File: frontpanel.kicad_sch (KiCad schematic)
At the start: 17 parts, among them M2 Pico_Display_Pack, Q6 Si2306BDS, SW1 STOP_SW, SW2 Rotary Enc EC11E, U9 MCP23017_SO

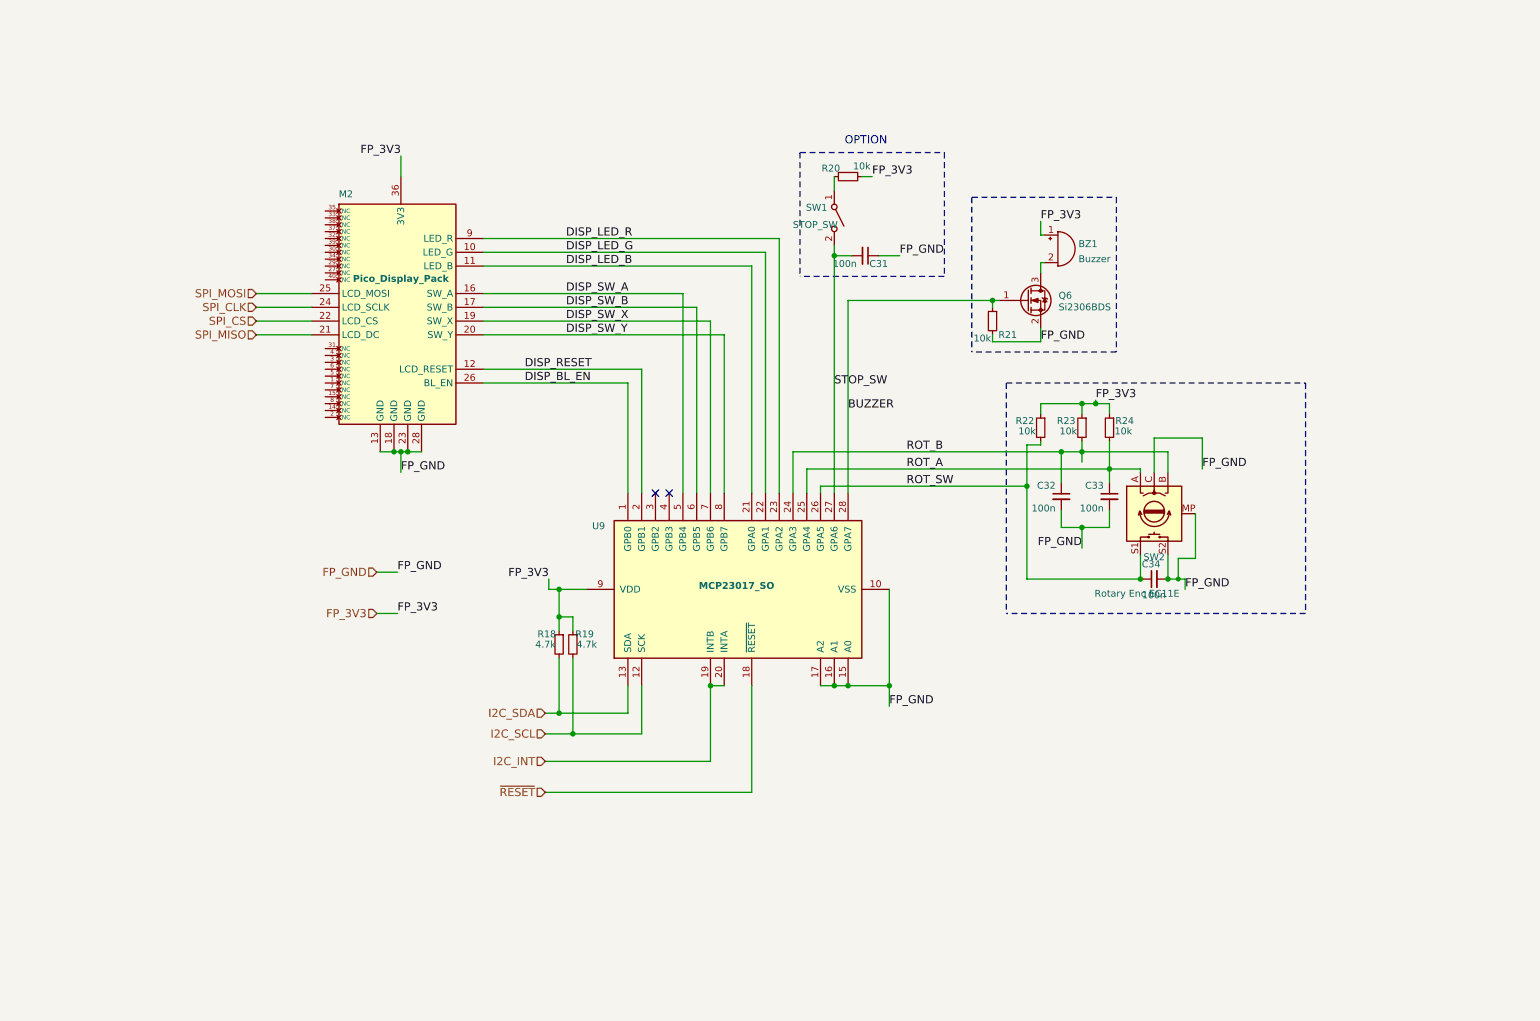
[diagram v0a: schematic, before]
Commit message: Update for Kicad 6-rc; replace 12V reg and cascade; add EEPROM;
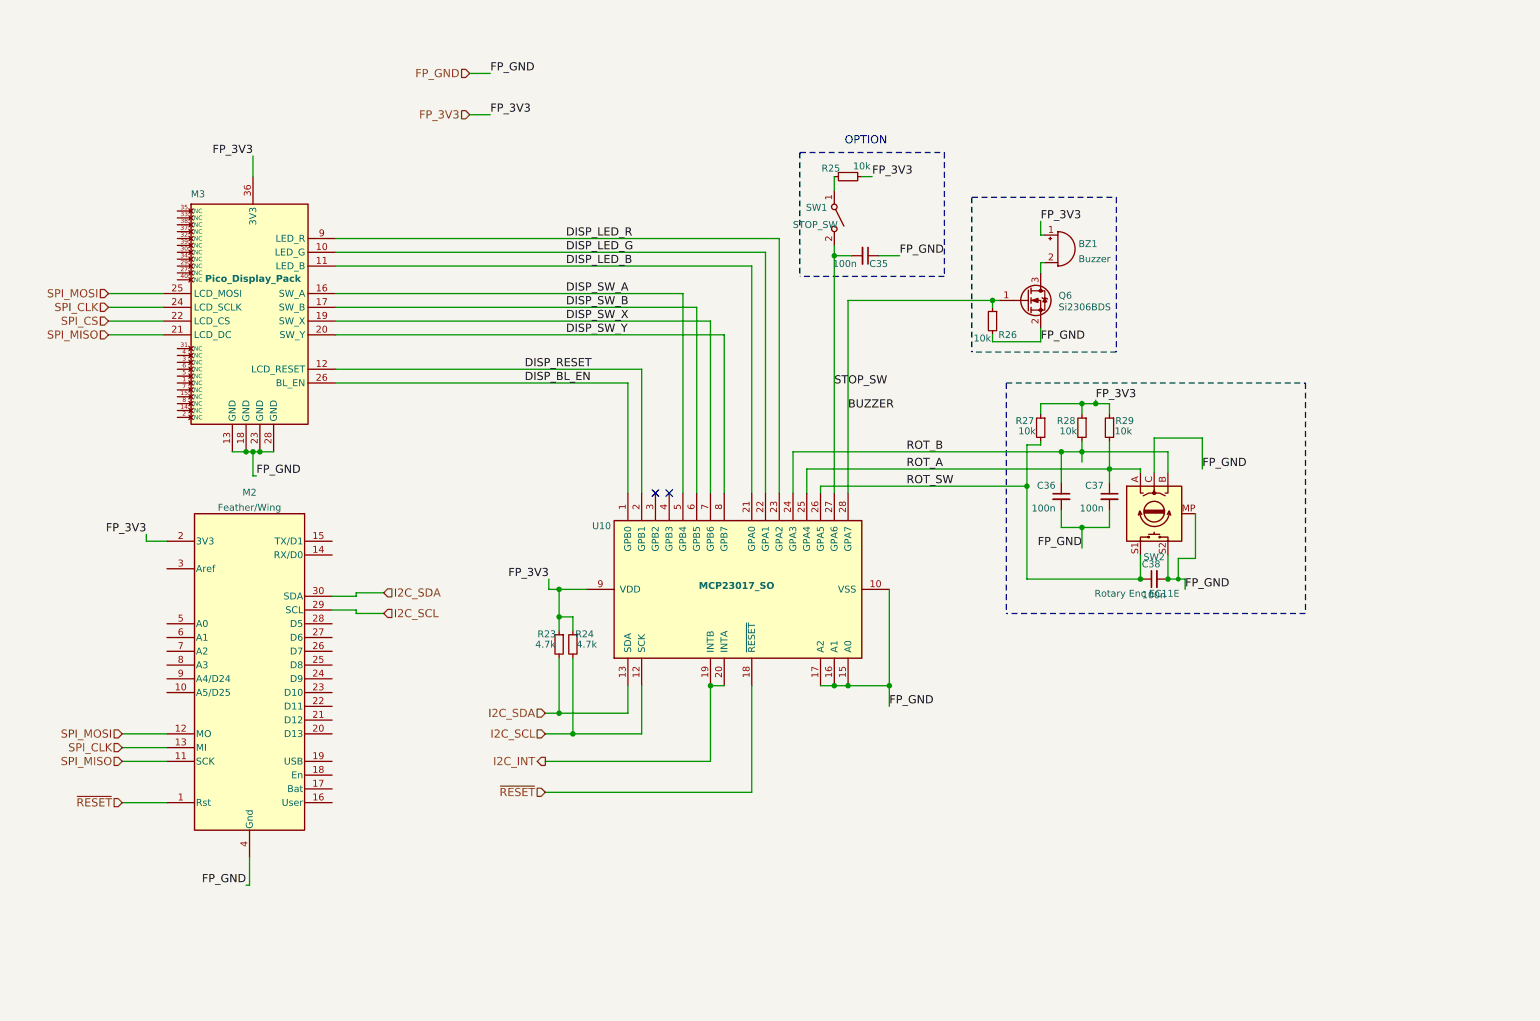
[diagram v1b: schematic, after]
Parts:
- added M2: Feather/Wing, solarpump:FeatherWing_Socket, symbol solarpump:Feather/Wing
- renumbered C31 to C35, C32 to C36, C33 to C37, C34 to C38, M2 to M3, R18 to R23, R19 to R24, R20 to R25, R21 to R26, R22 to R27, R23 to R28, R24 to R29, U9 to U10
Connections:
- net FP_3V3: now also M2.2 (3V3)
- net FP_GND: now also M2.4 (Gnd)
- net I2C_SCL: now also M2.29 (SCL)
- net I2C_SDA: now also M2.30 (SDA)
- net SPI_CLK: now also M2.13 (MI)
- net SPI_MISO: now also M2.11 (SCK)
- net SPI_MOSI: now also M2.12 (MO)
- net ~{RESET}: now also M2.1 (Rst)
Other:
- moved on the sheet: M3

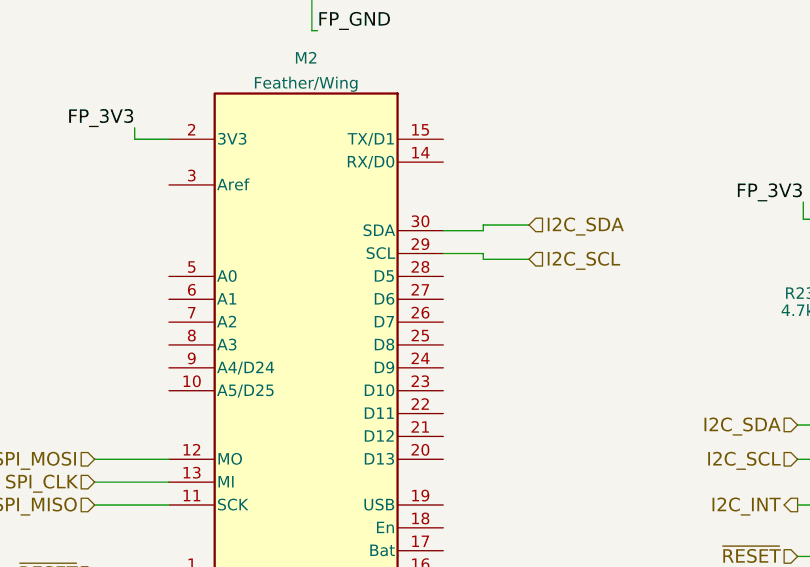
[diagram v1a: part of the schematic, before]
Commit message: Various important tweaks and fixes.
Fix several incorrect capacitor footprints;
Fix slightly incorrect footprint for USB connector;
Add ground vias around MPPT circuit;
Add Zener protection circuit for regulation error input;
Use pin header not socket for Pico Display header;
Fix missing connection to featherwing i2c;
Add in 3d models for USB socket and switch
Update kicad sheet dates;
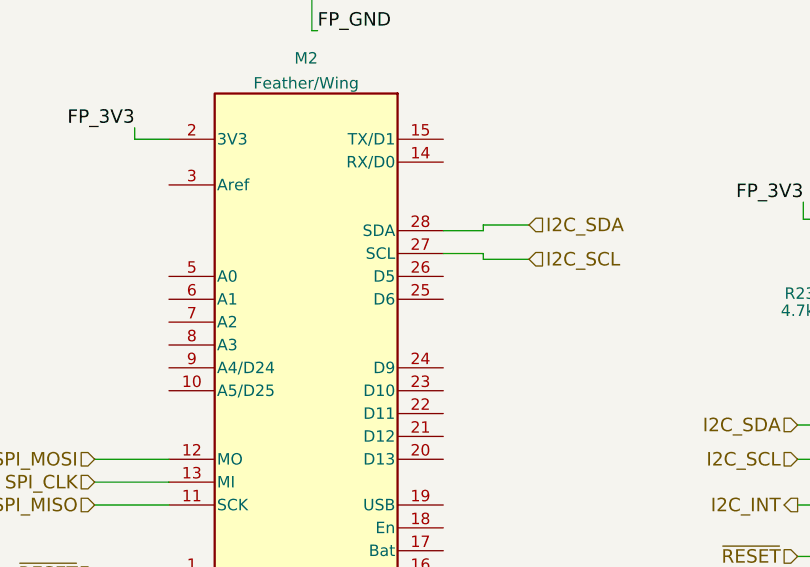
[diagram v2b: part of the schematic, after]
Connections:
- net I2C_SCL: now also M2.27 (SCL); no longer M2.29 (SCL)
- net I2C_SDA: now also M2.28 (SDA); no longer M2.30 (SDA)
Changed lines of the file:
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@@
   (title_block
     (title "SolarPump v3")
-    (date "2021-11-15")
+    (date "2021-12-03")
     (rev "1.0")
     (company "IvimeyCom")
@@
     (pin "27")
     (pin "28")
-    (pin "29")
     (pin "3")
-    (pin "30")
     (pin "4")
     (pin "5")

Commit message: Adjust footprint silkscreen; modify EC11 FP to inset into board, and adjust display board
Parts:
- SW2: footprint Rotary_Encoder:RotaryEncoder_Alps_EC11E-Switch_Vertical_H20mm -> solarpump:RotaryEncoder_Alps_EC11E-Switch_Vertical_H20mm_Inset
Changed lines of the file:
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@@
     (property "Reference" "SW2" (id 0) (at 224.155 113.4068 90))
     (property "Value" "Rotary Enc EC11E" (id 1) (at 220.98 120.1505 90))
-    (property "Footprint" "Rotary_Encoder:RotaryEncoder_Alps_EC11E-Switch_Vertical_H20mm" (id 2) (at 220.345 101.346 0)
+    (property "Footprint" "solarpump:RotaryEncoder_Alps_EC11E-Switch_Vertical_H20mm_Inset" (id 2) (at 220.345 101.346 0)
       (effects (font (size 1.27 1.27)) hide)
     )

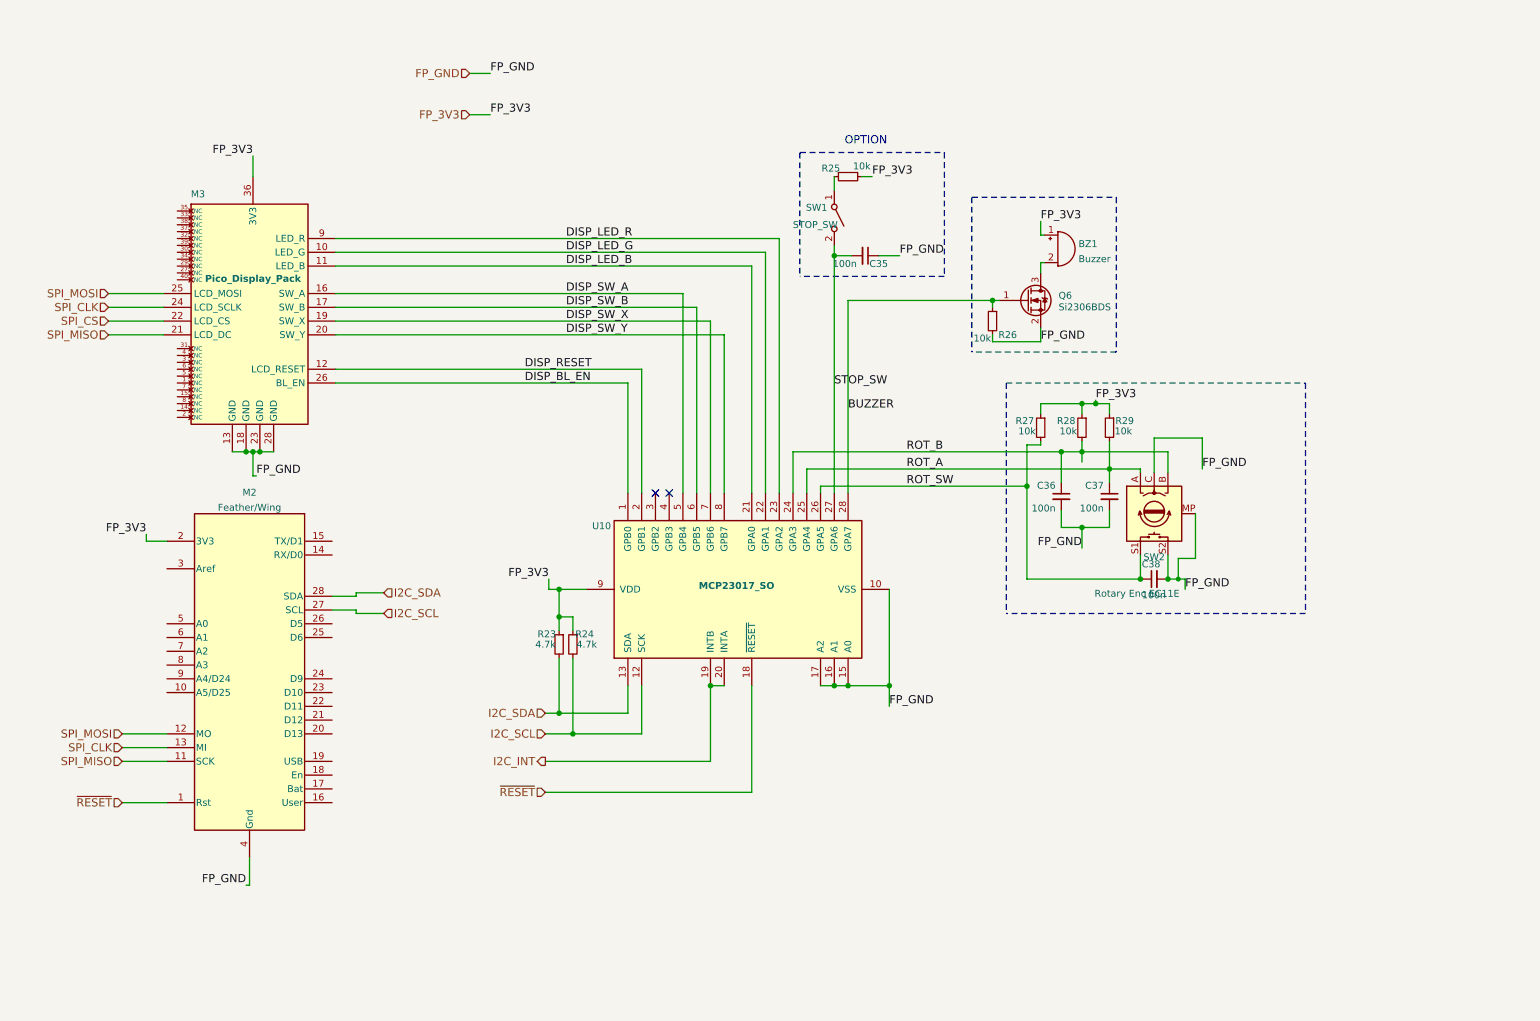
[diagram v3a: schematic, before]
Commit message: Rework with larger display; update component selection; add SWD conn; add RTC chip and QWIIC i2c socket
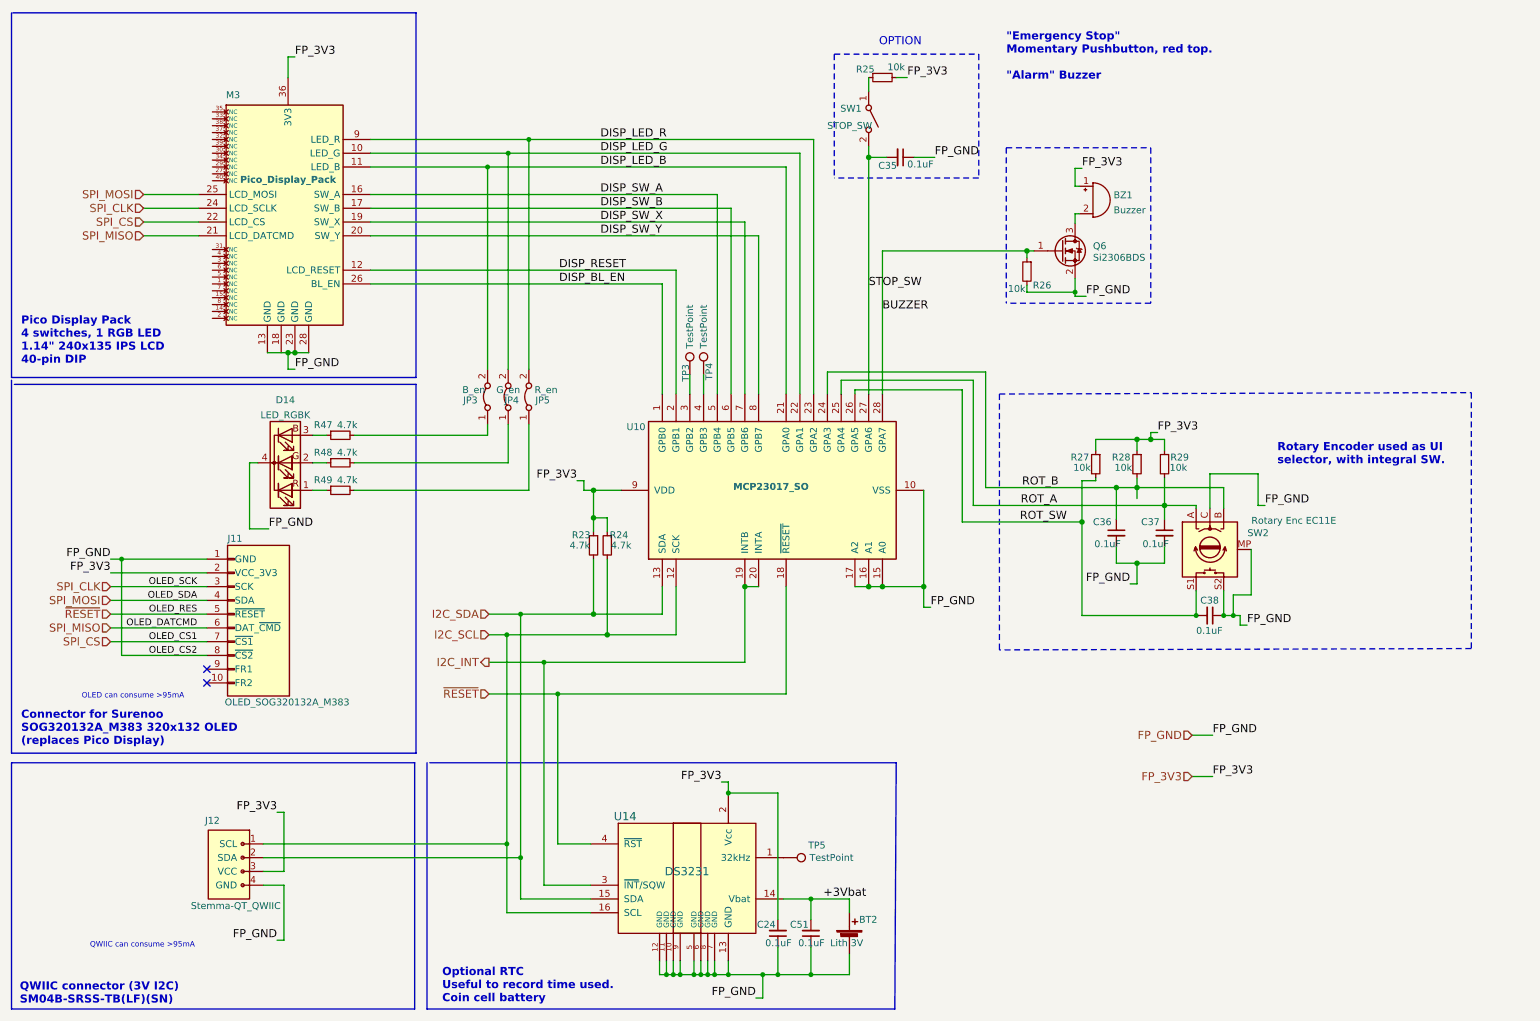
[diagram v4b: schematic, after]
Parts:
- removed M2: Feather/Wing, solarpump:FeatherWing_Socket, symbol solarpump:Feather/Wing
- added BT2: Lith 3V, Battery:BatteryHolder_Keystone_500, symbol Device:Battery_Cell
- added C24, C51: 0.1uF, Capacitor_SMD:C_0805_2012Metric_Pad1.18x1.45mm_HandSolder, symbol Device:C_Small
- added D14: LED_RGBK, LED_THT:LED_D5.0mm-4_RGB_Wide_Pins, symbol Device:LED_RGBK
- added J11: OLED_SOG320132A_M383, solarpump:OLED_SOG320132A_M383, symbol solarpump:OLED_SOG320132A_M383
- added J12: Stemma-QT_QWIIC, solarpump:STEMMA-QT_JSTS4B_PH-P2.00mm_Horizontal, symbol solarpump:Stemma-QT_QWIIC
- added JP3: B_en, Jumper:SolderJumper-2_P1.3mm_Bridged_Pad1.0x1.5mm, symbol Jumper:Jumper_2_Bridged
- added JP4: G_en, Jumper:SolderJumper-2_P1.3mm_Bridged_Pad1.0x1.5mm, symbol Jumper:Jumper_2_Bridged
- added JP5: R_en, Jumper:SolderJumper-2_P1.3mm_Bridged_Pad1.0x1.5mm, symbol Jumper:Jumper_2_Bridged
- added R47, R48, R49: 4.7k, Resistor_SMD:R_0805_2012Metric_Pad1.20x1.40mm_HandSolder, symbol Device:R_Small
- added TP3, TP4, TP5: TestPoint, TestPoint:TestPoint_Pad_1.0x1.0mm, symbol Connector:TestPoint
- added U14: DS3231, Package_SO:SOIC-16W_7.5x10.3mm_P1.27mm, symbol hat-ic:DS3231
- C35, C36, C37, C38: value 100n -> 0.1uF; footprint Capacitor_THT:C_Disc_D5.0mm_W2.5mm_P5.00mm -> Capacitor_SMD:C_0805_2012Metric_Pad1.18x1.45mm_HandSolder; Mfr TDK -> Samsung Electro-Mechanics; Mfr Name (none) -> C0402C104K8R7411; Mfr Part (none) -> Mouser; Mfr Part No FG28X5R1H105KRT0 -> CL21B104KACNNND; Part (none) -> 0.016; Price (none) -> KEMET; Repr-Cost (none) -> C0402C104K8R7411; Stock Number (none) -> Mouser; Supl Part No 810-FG28X5R1H105KRT0 -> 187-CL21B104KACNNND; Supl Price 0.297 -> 0.027
- M3: Mfr Pimoroni -> ThePiHut
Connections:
- net DISP_LED_B: now also JP3.2 (B)
- net DISP_LED_G: now also JP4.2 (B)
- net DISP_LED_R: now also JP5.2 (B)
- net FP_3V3: now also C24.2, J11.2 (VCC_3V3), J12.3 (VCC), U14.2 (Vcc)
- net FP_GND: now also C38.1, BT2.2 (-), C24.1, C51.1, D14.4 (K), J11.1 (GND), J11.8 (~{CS2}), J12.4 (GND), U14.10 (GND), U14.11 (GND), U14.12 (GND), U14.13 (GND), U14.5 (GND), U14.6 (GND), U14.7 (GND), U14.8 (GND), U14.9 (GND); no longer C38.2, M3.18 (GND)
- net I2C_INT: now also U14.3 (~{INT}/SQW)
- net I2C_SCL: now also J12.1 (SCL), U14.16 (SCL)
- net I2C_SDA: now also J12.2 (SDA), U14.15 (SDA)
- net ROT_SW: now also C38.2; no longer C38.1
- net SPI_CLK: now also J11.3 (SCK)
- net SPI_CS: now also J11.7 (~{CS1})
- net SPI_MISO: now also J11.6 (DAT_~{CMD})
- net SPI_MOSI: now also J11.4 (SDA)
- net ~{RESET}: now also J11.5 (~{RESET}), U14.4 (~{RST})
- net at U10.3 (GPB2): now also TP3.1
- net at U10.4 (GPB3): now also TP4.1
- new net: TP5.1, U14.1 (32kHz)
- new net: D14.1 (RA), R49.1
- new net: JP5.1 (A), R49.2
- new net: D14.3 (BA), R47.1
- new net: JP3.1 (A), R47.2
- new net: D14.2 (GA), R48.1
- new net: JP4.1 (A), R48.2
- new net +3Vbat: BT2.1 (+), C51.2, U14.14 (Vbat)
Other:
- note added: ""Emergency Stop" Momentary Pushbutton, red top. "Alarm" Buzzer"
- note added: "Connector for Surenoo SOG320132A_M383 320x132 OLED (replaces Pico Display)"
- note added: "OLED can consume >95mA"
- note added: "Optional RTC Useful to record time used. Coin cell battery"
- note added: "Pico Display Pack 4 switches, 1 RGB LED 1.14" 240x135 IPS LCD 40-pin DIP"
- note added: "QWIIC can consume >95mA"
- note added: "QWIIC connector (3V I2C) SM04B-SRSS-TB(LF)(SN)"
- note added: "Rotary Encoder used as UI selector, with integral SW."
- moved on the sheet: BZ1, M3, Q6, R23, R24, R25, R26, R27, R28, R29, SW1, SW2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
